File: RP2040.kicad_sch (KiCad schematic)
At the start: 34 parts, among them J3 USB_C_Receptacle_USB2.0_16P, SW1 SW_Push, U1 RP2040, U2 AMS1117-3.3, U4 W25Q16JVSS, Y1 X322512MSB4SI

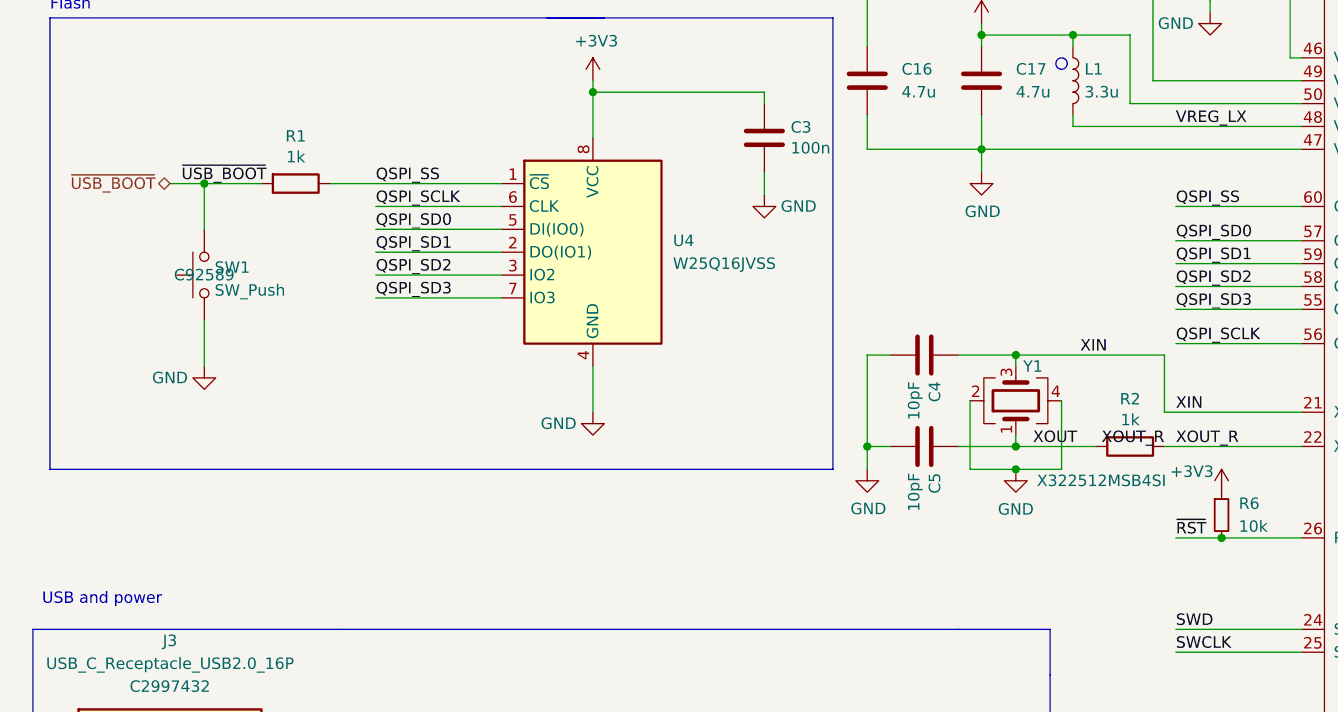
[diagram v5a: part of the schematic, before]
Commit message: add LED, make board smaller
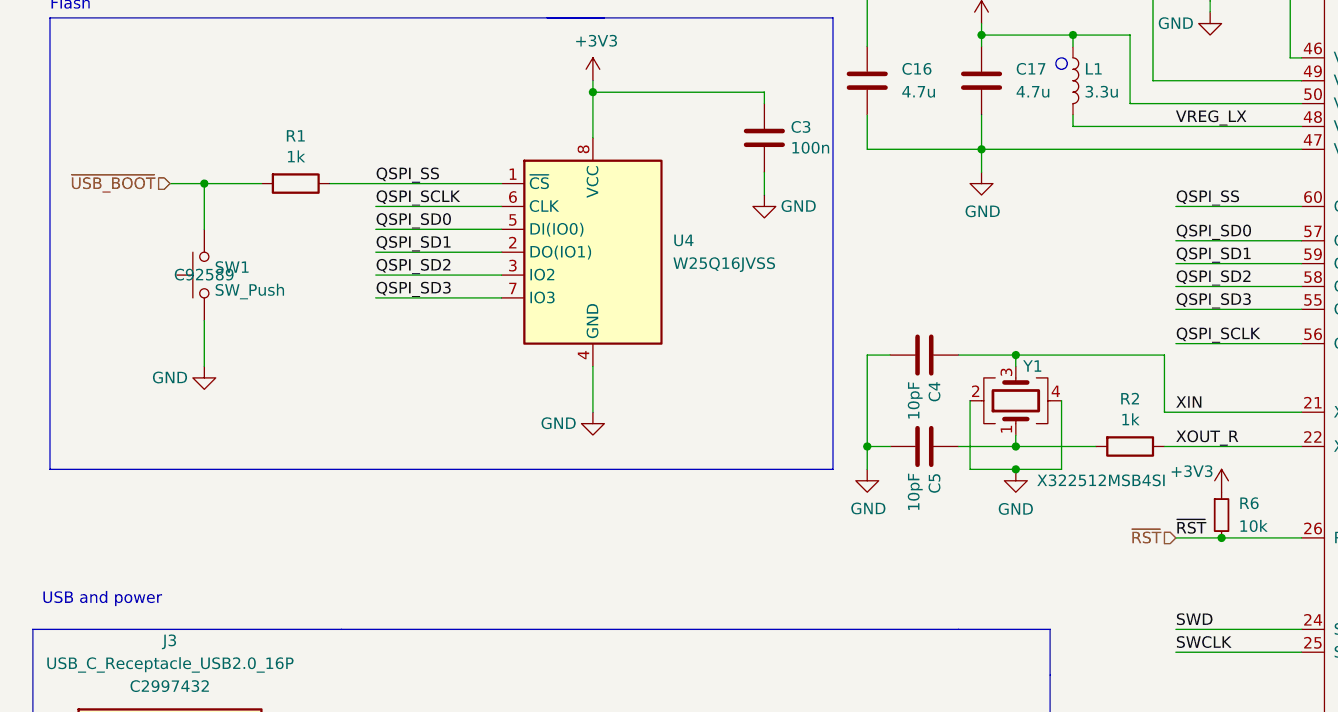
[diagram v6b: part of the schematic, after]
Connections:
- net XOUT: no longer names the net of C5.1, R2.2, Y1.1
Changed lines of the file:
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@@
-		)
-	)
-	(label "XOUT"
-		(at 126.365 116.84 0)
-		(effects
-			(font
-				(size 1.27 1.27)
-			)
-			(justify left bottom)
 		)
 	)
@@
 		)
 	)
-	(label "~{USB_BOOT}"
-		(at 31.75 87.63 0)
-		(effects
-			(font
-				(size 1.27 1.27)
-			)
-			(justify left bottom)
-		)
-	)
 	(label "~{RST}"
 		(at 142.24 127 0)
@@
 			)
 			(justify left bottom)
-		)
-	)
-	(label "XOUT_R"
-		(at 140.97 116.84 180)
-		(effects
-			(font
-				(size 1.27 1.27)
-			)
-			(justify right bottom)
-		)
-	)
-	(label "XIN"
-		(at 134.62 106.68 180)
-		(effects
-			(font
-				(size 1.27 1.27)
-			)
-			(justify right bottom)
 		)
 	)
@@
 		)
 	)
+	(hierarchical_label "~{RST}"
+		(shape input)
+		(at 142.24 127 180)
+		(effects
+			(font
+				(size 1.27 1.27)
+			)
+			(justify right)
+		)
+	)
 	(hierarchical_label "GPIO24"
 		(shape bidirectional)
@@
 	)
 	(hierarchical_label "~{USB_BOOT}"
-		(shape bidirectional)
+		(shape input)
 		(at 30.48 87.63 180)
 		(effects

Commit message: update production files acc. order
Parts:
- Y1: MPN - JLCPCB C9002 -> C20625731
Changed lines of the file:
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@@
 			)
 		)
-		(property "MPN - JLCPCB" "C9002"
+		(property "MPN - JLCPCB" "C20625731"
 			(at 124.46 111.76 0)
 			(effects

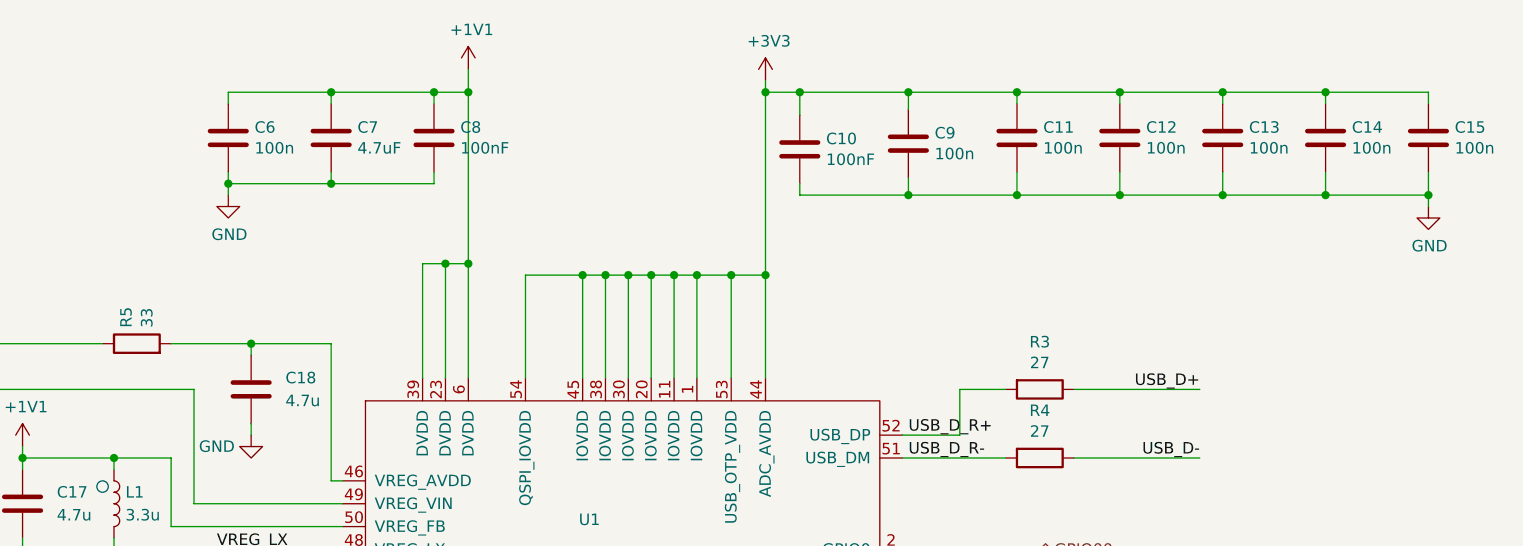
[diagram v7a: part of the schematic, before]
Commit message: add cap for AVDD, fix wrong cap value 1V1
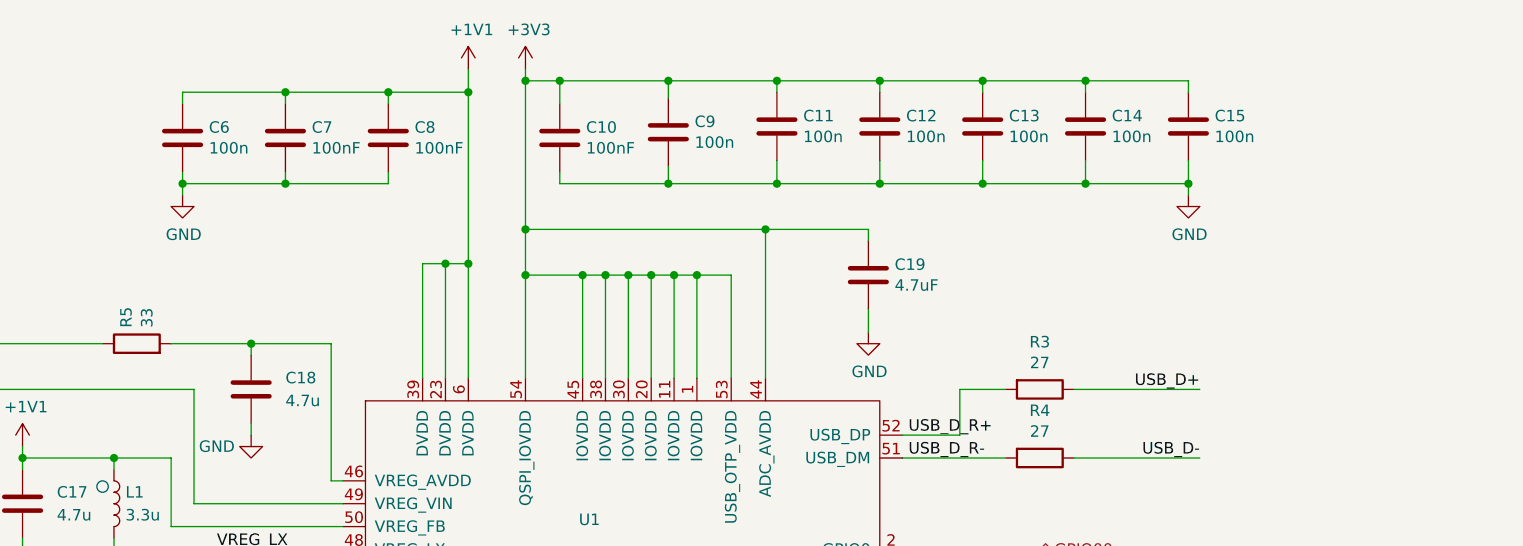
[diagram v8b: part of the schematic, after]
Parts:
- added C19: 4.7uF, Capacitor_SMD:C_0402_1005Metric, symbol Device:C
- C7: value 4.7uF -> 100nF
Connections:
- net +3V3: now also C19.1
- net GND: now also C19.2
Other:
- moved on the sheet: C10, C11, C12, C13, C14, C15, C6, C7, C8, C9
